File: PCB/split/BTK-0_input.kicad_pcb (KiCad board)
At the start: 4 copper layers, 139.5 x 105 mm, 66 parts, among them J7 Conn_01x16_Socket, SW10 1,2, SW11 2,2, SW12 3,2, SW13 4,2, SW14 5,2, SW15 6,2, SW16 1,3, SW17 2,3, SW18 3,3, SW19 4,3, SW20 5,3, SW21 6,3, SW22 1,4, SW23 2,4, SW24 3,4, SW25 4,4, SW26 5,4, SW27 6,4, SW28 1,4, SW29 2,4, SW3 RotaryEncoder_Switch_MP, SW30 3,4, SW31 4,4, SW32 5,4, SW33 6,4, SW4 1,1, SW5 2,1, SW6 3,1, SW7 4,1, SW8 5,1, SW9 6,1

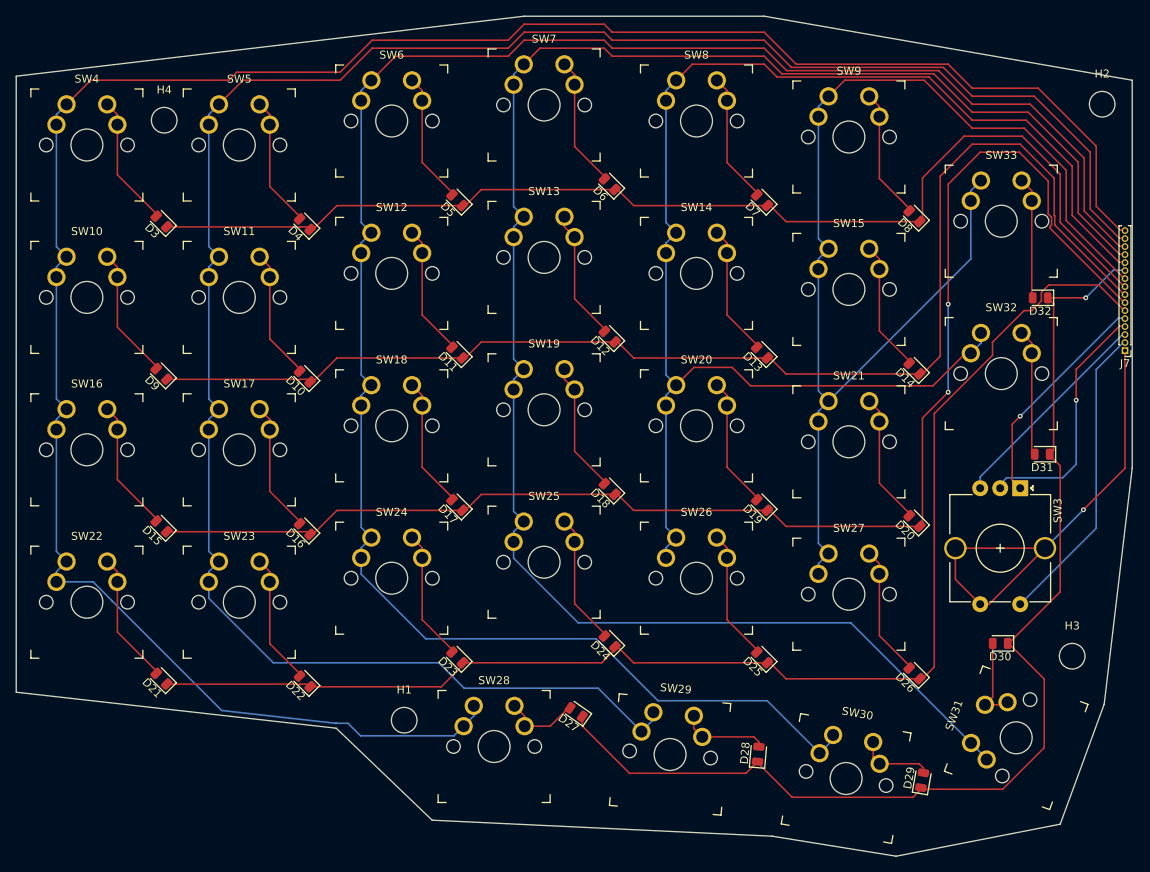
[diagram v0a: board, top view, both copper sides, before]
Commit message: separate split pcb production files created
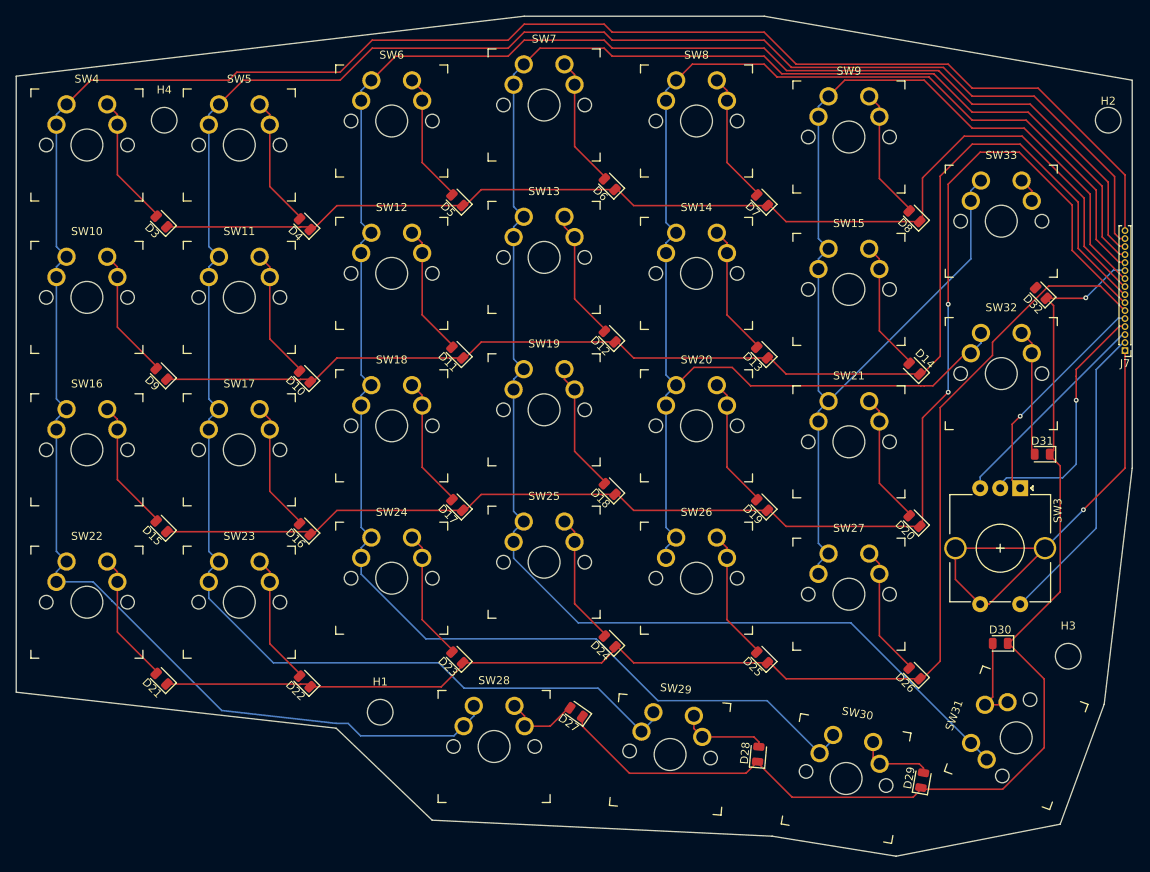
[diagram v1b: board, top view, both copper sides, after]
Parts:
- moved H1 3.16 mm to (27.0, 74.0)
- moved H2 2.14 mm to (118.0, 0.00)
- moved D32 0.61 mm to (109.6, 21.6), turned to 135 degrees
- moved H3 0.50 mm to (113.0, 67.0)
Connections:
- D10 pad 1: /IO14 -> /IO15
- D11 pad 1: /IO14 -> /IO15
- D12 pad 1: /IO14 -> /IO15
- D13 pad 1: /IO14 -> /IO15
- D14 pad 1: /IO14 -> /IO15
- D15 pad 1: /IO15 -> /IO18
- D16 pad 1: /IO15 -> /IO18
- D17 pad 1: /IO15 -> /IO18
- D18 pad 1: /IO15 -> /IO18
- D19 pad 1: /IO15 -> /IO18
- D20 pad 1: /IO15 -> /IO18
- D21 pad 1: /IO18 -> /IO19
- D22 pad 1: /IO18 -> /IO19
- D23 pad 1: /IO18 -> /IO19
- D24 pad 1: /IO18 -> /IO19
- D25 pad 1: /IO18 -> /IO19
- D26 pad 1: /IO18 -> /IO19
- D3 pad 1: /IO7 -> /IO14
- D4 pad 1: /IO7 -> /IO14
- D5 pad 1: /IO7 -> /IO14
- D6 pad 1: /IO7 -> /IO14
- D7 pad 1: /IO7 -> /IO14
- D8 pad 1: /IO7 -> /IO14
- D9 pad 1: /IO14 -> /IO15
- J7 pad 10: /IO19 -> /IO7
- J7 pad 6: /IO18 -> /IO19
- J7 pad 7: /IO15 -> /IO18
- J7 pad 8: /IO14 -> /IO15
- J7 pad 9: /IO7 -> /IO14
- SW15 pad 1: /IO19 -> /IO7
- SW21 pad 1: /IO19 -> /IO7
- SW27 pad 1: /IO19 -> /IO7
- SW33 pad 1: /IO19 -> /IO7
- SW9 pad 1: /IO19 -> /IO7
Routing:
- net /IO15: track 177.0 -> 159.5 mm, vias 2 -> 0
- net /IO14: track 159.5 -> 142.2 mm
- net /IO19: track 150.6 -> 164.5 mm
- net Net-(D32-A): track 15.2 -> 3.07 mm
- net /IO18: track 165.1 -> 176.8 mm, vias 0 -> 2
- net /IO7: track 142.2 -> 150.6 mm
